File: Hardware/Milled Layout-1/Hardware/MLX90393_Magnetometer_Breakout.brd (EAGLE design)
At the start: 20.3 x 20.3 mm, 16 parts, among them U1 MLX90393_MAGNETOMETER

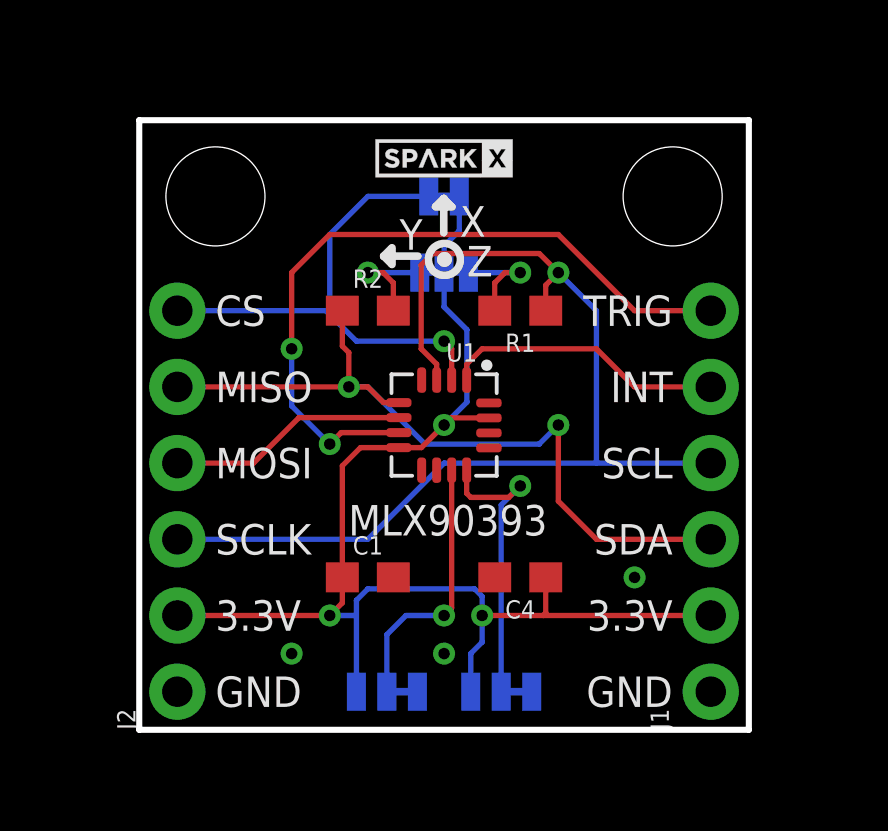
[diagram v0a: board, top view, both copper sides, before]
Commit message: Adding new panel with updated silk and cream
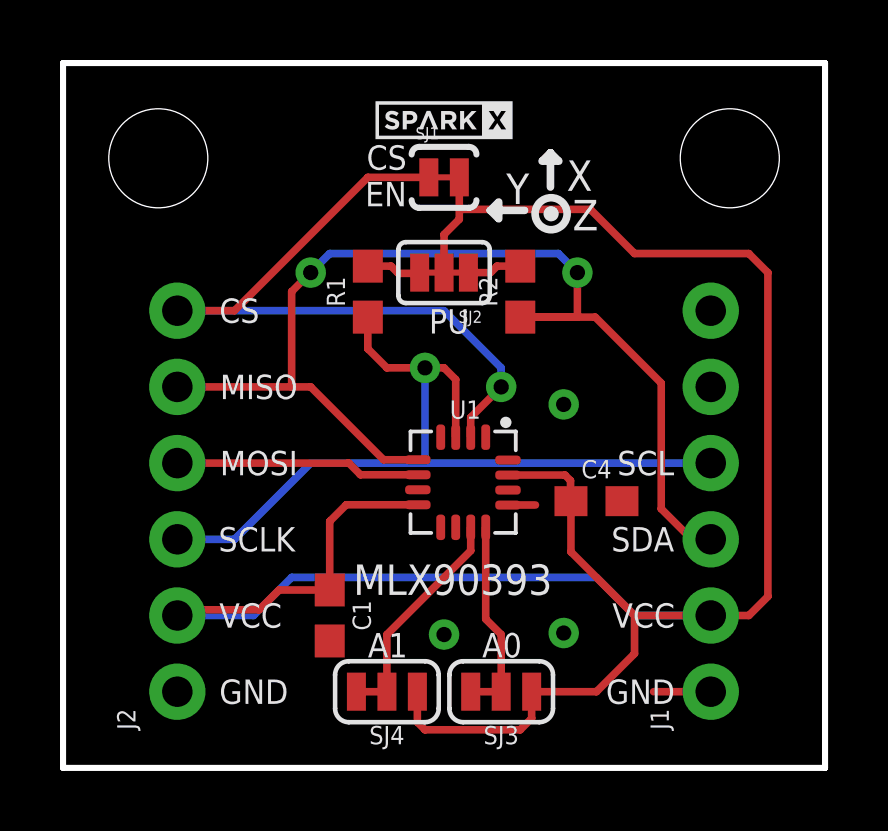
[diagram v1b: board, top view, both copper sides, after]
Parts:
- SJ1: device SparkFun-Jumpers:SMT-JUMPER_2_NC_TRACE_SILK -> SparkFun:SJ_2S-TRACE
- moved U$1 24.5 mm to (-13.3, -0.64)
- moved R1 5.12 mm to (7.62, 14.6), turned to 90 degrees
- moved R2 5.12 mm to (12.7, 14.6), turned to 90 degrees
- moved C4 3.59 mm to (15.2, 7.62), turned to 0 degrees
- moved JP3 2.29 mm to (0.64, 19.1)
- moved JP4 2.29 mm to (19.7, 19.1)
- moved U1 2.01 mm to (10.8, 8.26)
- moved C1 1.80 mm to (6.35, 3.81), turned to 270 degrees
- moved U$2 1.27 mm to (10.2, 20.3)
- moved SJ1 0.63 mm to (10.2, 18.4), flipped to the top, turned to 0 degrees
- flipped SJ2 to the top
- flipped SJ3 to the top
- flipped SJ4 to the top
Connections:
- net 3.3V renamed VDD
- net INT: no longer J1.5
- net TRIG: no longer J1.6
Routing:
- net VDD: track 44.9 -> 78.5 mm, vias 3 -> 0
- net TRIG: track 24.2 -> 0.00 mm, vias 2 -> 0
- net SDA: track 26.4 -> 37.8 mm
- net INT: track 9.40 -> 0.00 mm
- net SCL: track 36.2 -> 28.3 mm
- net CS: track 17.2 -> 24.5 mm
- net A0: track 9.89 -> 5.69 mm, vias 1 -> 0
- net GND: track 0.00 -> 2.79 mm
- net A1: track 9.02 -> 6.64 mm, vias 1 -> 0
- net N$4: track 3.65 -> 1.82 mm, vias 1 -> 0
- net N$5: track 3.65 -> 1.84 mm, vias 1 -> 0
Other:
- board size 20.3 x 20.3 mm -> 25.4 x 23.5 mm
- board text added: "CS EN"
- board text added: "VCC"
- board text removed: "3.3V"
- board text removed: "INT"
- board text removed: "J. Bartlett"
- board text removed: "TRIG"
